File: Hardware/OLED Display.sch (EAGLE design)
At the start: 26 parts, among them J1 QWIIC_RIGHT_ANGLE, J3 QWIIC_RIGHT_ANGLE, U1 QG-2832TLBFG02

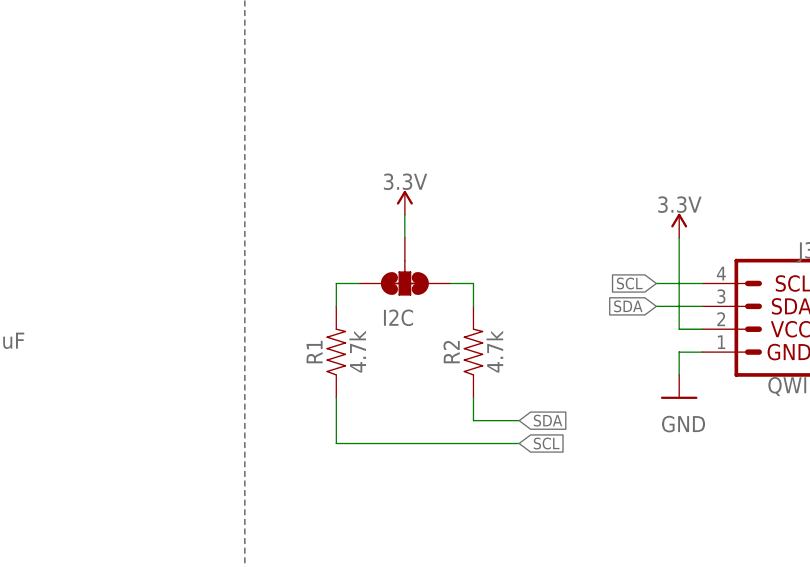
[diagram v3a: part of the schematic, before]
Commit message: Shrinks the overall size of the board
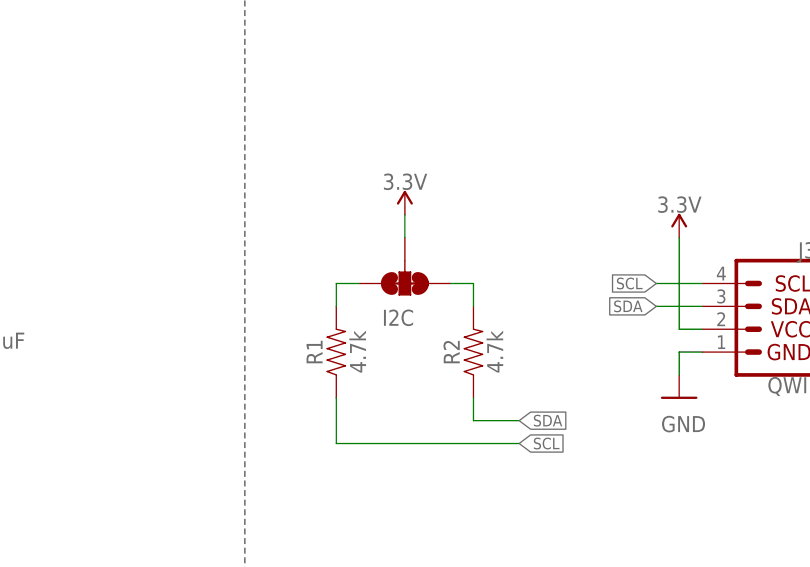
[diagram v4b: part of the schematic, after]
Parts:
- I2C: value SMT-JUMPER_3_2-NC_TRACE -> JUMPER-SMT_3_2-NC_TRACE_SILK; device NOA-Jumpers:SMT-JUMPER_3_2-NC_TRACE -> SparkFun-Jumpers:JUMPER-SMT_3_2-NC_TRACE_SILK
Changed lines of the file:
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@@
 <part name="GND8" library="SparkFun-PowerSymbols" deviceset="GND" device=""/>
 <part name="GND9" library="SparkFun-PowerSymbols" deviceset="GND" device=""/>
-<part name="I2C" library="NOA-Jumpers" deviceset="SMT-JUMPER_3_2-NC_TRACE" device=""/>
+<part name="I2C" library="SparkFun-Jumpers" deviceset="JUMPER-SMT_3_2-NC_TRACE" device="_SILK" package3d_urn="urn:adsk.eagle:package:39289/1"/>
 <part name="LOGO2" library="OSHW-LOGO-M" deviceset="OSHW-LOGO" device="MINI"/>
 <part name="FRAME2" library="SparkFun-Aesthetics" deviceset="FRAME-LETTER" device="">
@@
 will not be understood (or retained) with this version.
 </note>
+<note version="8.3" severity="warning">
+Since Version 8.3, EAGLE supports the association of 3D packages
+with devices in libraries, schematics, and board files. Those 3D
+packages will not be understood (or retained) with this version.
+</note>
 </compatibility>

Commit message: Routes the board
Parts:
- removed C3: 1.0uF, SparkFun-Capacitors:1.0UF-0603-16V-10%
- removed U1: QG-2832TLBFG02, Module:OLED-12832
- added U2: APX803S-SA, Module:APX803S-SA
- added U3: OLED_0.9"-QG-2832TLBFG02, Module:OLED_0.9"-QG-2832TLBFG02
- LOGO1: value SFE_LOGO_NAME_FLAME.2_INCH -> SFE_LOGO_NAME_FLAME.1_INCH; device SparkFun-Aesthetics:SFE_LOGO_NAME_FLAME.2_INCH -> SparkFun-Aesthetics:SFE_LOGO_NAME_FLAME.1_INCH
- R4: value 100k -> 10k; device SparkFun-Resistors:100KOHM-0603-1/10W-1% -> SparkFun-Resistors:10KOHM-0603-1/10W-1%
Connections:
- removed net N$3: C2.2, U1.C1P
- new net N$17: C2.1, U3.C2N
- net 3.3V: now also U2.VCC, U3.VBAT, U3.VDD; no longer U1.VBAT, U1.VDD
- net GND: now also U2.GND, U3.VSS; no longer C3.2, U1.VSS
- net N$1: now also C2.2, U3.C2P; no longer C1.2, U1.C2P
- net N$2: now also U3.C1N; no longer U1.C2N
- net N$4: now also C1.2, U3.C1P; no longer C2.1, U1.C1N
- net N$6: now also U3.VCOMH; no longer U1.VCOMH
- net N$7: now also U3.VCC; no longer U1.VCC
- net N$9: now also U3.IREF; no longer U1.IREF
- net RST: now also U2.!RST!, U3.RST; no longer C3.1, U1.RES#
- net SCL: now also U3.SCL; no longer U1.SCL
- net SDA: now also U3.SDA; no longer U1.SDA
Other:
- note added: "Soft Start Circuit - APX803S-SA"
- note removed: "100ms Delayed Startup"
- note removed: "Soft Start Circuit"
- moved on the sheet: C1, C2, C4, C5, C7, C8, R3, R4

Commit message: Updates the display device and footprint name, adds version in silk
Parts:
- U3: value OLED_0.9"-QG-2832TLBFG02 -> QG-2832TLBFG02; device Module:OLED_0.9"-QG-2832TLBFG02 -> Module:QG-2832TLBFG02
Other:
- moved on the sheet: C7
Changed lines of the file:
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@@
 <part name="SUPPLY6" library="SparkFun-PowerSymbols" deviceset="3.3V" device=""/>
 <part name="LOGO1" library="SparkFun-Aesthetics" deviceset="SFE_LOGO_NAME_FLAME" device=".1_INCH"/>
-<part name="U3" library="Module" deviceset="OLED_0.9&quot;-QG-2832TLBFG02" device=""/>
+<part name="U3" library="Module" deviceset="QG-2832TLBFG02" device=""/>
 <part name="GND16" library="SparkFun-PowerSymbols" deviceset="GND" device=""/>
 </parts>
@@
 <instance part="H2" gate="G$1" x="238.76" y="30.48" smashed="yes"/>
 <instance part="LOGO3" gate="G$1" x="157.48" y="40.64" smashed="yes"/>
-<instance part="C7" gate="G$1" x="27.94" y="129.54" smashed="yes" rot="MR180">
-<attribute name="NAME" x="28.321" y="133.096" size="1.778" layer="95" font="vector" rot="R270"/>
-<attribute name="VALUE" x="28.321" y="118.364" size="1.778" layer="96" font="vector" rot="MR90"/>
+<instance part="C7" gate="G$1" x="27.94" y="127" smashed="yes" rot="MR180">
+<attribute name="NAME" x="28.321" y="130.556" size="1.778" layer="95" font="vector" rot="R270"/>
+<attribute name="VALUE" x="28.321" y="115.824" size="1.778" layer="96" font="vector" rot="MR90"/>
 </instance>
 <instance part="C8" gate="G$1" x="17.78" y="144.78" smashed="yes" rot="MR180">
@@
 <attribute name="VALUE" x="22.86" y="114.046" size="1.778" layer="96" font="vector" rot="MR0" align="top-center"/>
 </instance>
-<instance part="SUPPLY1" gate="G$1" x="17.78" y="172.72" smashed="yes" rot="MR0">
-<attribute name="VALUE" x="17.78" y="175.514" size="1.778" layer="96" font="vector" rot="MR0" align="bottom-center"/>
+<instance part="SUPPLY1" gate="G$1" x="17.78" y="152.4" smashed="yes" rot="MR0">
+<attribute name="VALUE" x="17.78" y="155.194" size="1.778" layer="96" font="vector" rot="MR0" align="bottom-center"/>
 </instance>
 <instance part="SUPPLY2" gate="G$1" x="134.62" y="149.86" smashed="yes">
@@
 <attribute name="VALUE" x="35.56" y="114.046" size="1.778" layer="96" font="vector" rot="MR0" align="top-center"/>
 </instance>
-<instance part="GND6" gate="1" x="73.66" y="104.14" smashed="yes">
-<attribute name="VALUE" x="73.66" y="103.886" size="1.778" layer="96" font="vector" align="top-center"/>
+<instance part="GND6" gate="1" x="73.66" y="114.3" smashed="yes">
+<attribute name="VALUE" x="73.66" y="114.046" size="1.778" layer="96" font="vector" align="top-center"/>
 </instance>
 <instance part="GND7" gate="1" x="17.78" y="114.3" smashed="yes" rot="MR0">
@@
 <segment>
 <pinref part="C7" gate="G$1" pin="1"/>
-<wire x1="27.94" y1="124.46" x2="27.94" y2="116.84" width="0.1524" layer="91"/>
+<wire x1="27.94" y1="121.92" x2="27.94" y2="116.84" width="0.1524" layer="91"/>
 <pinref part="GND4" gate="1" pin="GND"/>
 </segment>
@@
 <pinref part="GND6" gate="1" pin="GND"/>
 <pinref part="R3" gate="G$1" pin="1"/>
-<wire x1="73.66" y1="119.38" x2="73.66" y2="106.68" width="0.1524" layer="91"/>
+<wire x1="73.66" y1="119.38" x2="73.66" y2="116.84" width="0.1524" layer="91"/>
 </segment>
 <segment>
@@
 <net name="N$7" class="0">
 <segment>
-<wire x1="27.94" y1="134.62" x2="27.94" y2="132.08" width="0.1524" layer="91"/>
+<wire x1="27.94" y1="134.62" x2="27.94" y2="129.54" width="0.1524" layer="91"/>
 <pinref part="C7" gate="G$1" pin="2"/>
 <pinref part="U3" gate="G$1" pin="VCC"/>
@@
 <wire x1="17.78" y1="147.32" x2="17.78" y2="149.86" width="0.1524" layer="91" style="longdash"/>
 <junction x="17.78" y="149.86"/>
-<wire x1="17.78" y1="172.72" x2="17.78" y2="149.86" width="0.1524" layer="91"/>
+<wire x1="17.78" y1="152.4" x2="17.78" y2="149.86" width="0.1524" layer="91"/>
 <pinref part="SUPPLY1" gate="G$1" pin="3.3V"/>
 <pinref part="U3" gate="G$1" pin="VDD"/>

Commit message: Adds testpoints
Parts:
- added TP1, TP2, TP3, TP4: TEST-POINT3X4, SparkFun-Connectors:TEST-POINT3X4
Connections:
- net 3.3V: now also TP3.1
- net GND: now also TP4.1
- net SCL: now also TP1.1
- net SDA: now also TP2.1
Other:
- note added: "Testpoints"
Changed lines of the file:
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@@
 <part name="U3" library="Module" deviceset="QG-2832TLBFG02" device=""/>
 <part name="GND16" library="SparkFun-PowerSymbols" deviceset="GND" device=""/>
+<part name="TP1" library="SparkFun-Connectors" deviceset="TEST-POINT" device="3X4"/>
+<part name="TP2" library="SparkFun-Connectors" deviceset="TEST-POINT" device="3X4"/>
+<part name="TP3" library="SparkFun-Connectors" deviceset="TEST-POINT" device="3X4"/>
+<part name="TP4" library="SparkFun-Connectors" deviceset="TEST-POINT" device="3X4"/>
+<part name="SUPPLY7" library="SparkFun-PowerSymbols" deviceset="3.3V" device=""/>
+<part name="GND2" library="SparkFun-PowerSymbols" deviceset="GND" device=""/>
 </parts>
 <sheets>
@@
 <text x="149.86" y="7.62" size="2.54" layer="94" font="vector">Revised By: Elias Santistevan</text>
 <wire x1="116.84" y1="185.42" x2="116.84" y2="99.06" width="0.1524" layer="97" style="longdash"/>
-<wire x1="116.84" y1="99.06" x2="116.84" y2="0" width="0.1524" layer="97" style="longdash"/>
+<wire x1="116.84" y1="99.06" x2="116.84" y2="58.42" width="0.1524" layer="97" style="longdash"/>
+<wire x1="116.84" y1="58.42" x2="116.84" y2="0" width="0.1524" layer="97" style="longdash"/>
 <wire x1="0" y1="99.06" x2="116.84" y2="99.06" width="0.1524" layer="97" style="longdash"/>
-<wire x1="116.84" y1="99.06" x2="248.92" y2="99.06" width="0.1524" layer="97" style="longdash"/>
+<wire x1="116.84" y1="99.06" x2="160.02" y2="99.06" width="0.1524" layer="97" style="longdash"/>
 <text x="182.88" y="177.8" size="2.54" layer="94" font="vector" align="center">Qwiic Connectors</text>
 <text x="60.96" y="180.34" size="2.54" layer="94" font="vector" align="center">OLED Display - QG-2832TLBFG02</text>
 <text x="60.96" y="91.44" size="2.54" layer="94" font="vector" align="center">Soft Start Circuit - APX803S-SA</text>
+<text x="129.54" y="91.44" size="2.54" layer="94" font="vector">Testpoints</text>
+<wire x1="160.02" y1="99.06" x2="248.92" y2="99.06" width="0.1524" layer="97" style="longdash"/>
+<wire x1="116.84" y1="58.42" x2="160.02" y2="58.42" width="0.2032" layer="97" style="longdash"/>
+<wire x1="160.02" y1="58.42" x2="160.02" y2="99.06" width="0.2032" layer="97" style="longdash"/>
 </plain>
 <instances>
@@
 <attribute name="VALUE" x="43.18" y="114.046" size="1.778" layer="96" font="vector" rot="MR0" align="top-center"/>
 </instance>
+<instance part="TP1" gate="G$1" x="139.7" y="78.74" smashed="yes">
+<attribute name="NAME" x="144.78" y="78.74" size="1.778" layer="95" font="vector"/>
+</instance>
+<instance part="TP2" gate="G$1" x="139.7" y="76.2" smashed="yes">
+<attribute name="NAME" x="144.78" y="76.2" size="1.778" layer="95" font="vector"/>
+</instance>
+<instance part="TP3" gate="G$1" x="139.7" y="73.66" smashed="yes">
+<attribute name="NAME" x="144.78" y="73.66" size="1.778" layer="95" font="vector"/>
+</instance>
+<instance part="TP4" gate="G$1" x="139.7" y="71.12" smashed="yes">
+<attribute name="NAME" x="144.78" y="71.12" size="1.778" layer="95" font="vector"/>
+</instance>
+<instance part="SUPPLY7" gate="G$1" x="137.16" y="81.28" smashed="yes">
+<attribute name="VALUE" x="137.16" y="84.074" size="1.778" layer="96" font="vector" align="bottom-center"/>
+</instance>
+<instance part="GND2" gate="1" x="137.16" y="66.04" smashed="yes">
+<attribute name="VALUE" x="137.16" y="65.786" size="1.778" layer="96" font="vector" align="top-center"/>
+</instance>
 </instances>
 <busses>
@@
 <pinref part="GND16" gate="1" pin="GND"/>
 </segment>
+<segment>
+<pinref part="TP4" gate="G$1" pin="1"/>
+<wire x1="139.7" y1="71.12" x2="137.16" y2="71.12" width="0.1524" layer="91"/>
+<pinref part="GND2" gate="1" pin="GND"/>
+<wire x1="137.16" y1="71.12" x2="137.16" y2="68.58" width="0.1524" layer="91"/>
+</segment>
 </net>
 <net name="SCL" class="0">
@@
 <label x="162.56" y="142.24" size="1.27" layer="95" font="vector" rot="R180" xref="yes"/>
 </segment>
+<segment>
+<pinref part="TP1" gate="G$1" pin="1"/>
+<wire x1="139.7" y1="78.74" x2="134.62" y2="78.74" width="0.1524" layer="91"/>
+<label x="134.62" y="78.74" size="1.27" layer="95" rot="R180" xref="yes"/>
+</segment>
 </net>
 <net name="SDA" class="0">
@@
 <wire x1="167.64" y1="139.7" x2="162.56" y2="139.7" width="0.1524" layer="91"/>
 <label x="162.56" y="139.7" size="1.27" layer="95" font="vector" rot="R180" xref="yes"/>
+</segment>
+<segment>
+<pinref part="TP2" gate="G$1" pin="1"/>
+<wire x1="139.7" y1="76.2" x2="134.62" y2="76.2" width="0.1524" layer="91"/>
+<label x="134.62" y="76.2" size="1.27" layer="95" rot="R180" xref="yes"/>
 </segment>
 </net>
@@
 <pinref part="SUPPLY6" gate="G$1" pin="3.3V"/>
 </segment>
-</net>
+<segment>
+<pinref part="SUPPLY7" gate="G$1" pin="3.3V"/>
+<pinref part="TP3" gate="G$1" pin="1"/>
+<wire x1="139.7" y1="73.66" x2="137.16" y2="73.66" width="0.1524" layer="91"/>
+<wire x1="137.16" y1="73.66" x2="137.16" y2="81.28" width="0.1524" layer="91"/>
+</segment>
+</net>

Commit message: Adds more datasheets, updates part number for OLED display
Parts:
- U3: value QG-2832TLBFG02 -> AMO091-12832BFG02-H14; device Module:QG-2832TLBFG02 -> Module:AMO091-12832BFG02-H14
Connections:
- removed net RST: R4.1, U2.!RST!, U3.RST
- new net !RST!: R4.1, U2.!RST!, U3.!RST!
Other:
- note added: "OLED Display AMO091-12832BFG02-H14"
- note removed: "OLED Display - QG-2832TLBFG02"
- moved on the sheet: R3
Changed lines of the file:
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@@
 <part name="SUPPLY6" library="SparkFun-PowerSymbols" deviceset="3.3V" device=""/>
 <part name="LOGO1" library="SparkFun-Aesthetics" deviceset="SFE_LOGO_NAME_FLAME" device=".1_INCH"/>
-<part name="U3" library="Module" deviceset="QG-2832TLBFG02" device=""/>
+<part name="U3" library="Module" deviceset="AMO091-12832BFG02-H14" device=""/>
 <part name="GND16" library="SparkFun-PowerSymbols" deviceset="GND" device=""/>
 <part name="TP1" library="SparkFun-Connectors" deviceset="TEST-POINT" device="3X4"/>
@@
 <wire x1="116.84" y1="99.06" x2="160.02" y2="99.06" width="0.1524" layer="97" style="longdash"/>
 <text x="182.88" y="177.8" size="2.54" layer="94" font="vector" align="center">Qwiic Connectors</text>
-<text x="60.96" y="180.34" size="2.54" layer="94" font="vector" align="center">OLED Display - QG-2832TLBFG02</text>
+<text x="60.96" y="177.8" size="2.54" layer="94" font="vector" align="center">OLED Display
+AMO091-12832BFG02-H14
+</text>
 <text x="60.96" y="91.44" size="2.54" layer="94" font="vector" align="center">Soft Start Circuit - APX803S-SA</text>
 <text x="129.54" y="91.44" size="2.54" layer="94" font="vector">Testpoints</text>
@@
 <attribute name="VALUE" x="143.764" y="134.62" size="1.778" layer="96" font="vector" rot="R90" align="top-center"/>
 </instance>
-<instance part="R3" gate="G$1" x="73.66" y="124.46" smashed="yes" rot="R90">
-<attribute name="NAME" x="74.422" y="129.54" size="1.778" layer="95" font="vector" rot="R270" align="bottom-center"/>
-<attribute name="VALUE" x="76.2" y="118.364" size="1.778" layer="96" font="vector" rot="R270" align="top-center"/>
+<instance part="R3" gate="G$1" x="81.28" y="124.46" smashed="yes" rot="R90">
+<attribute name="NAME" x="82.042" y="129.54" size="1.778" layer="95" font="vector" rot="R270" align="bottom-center"/>
+<attribute name="VALUE" x="83.82" y="118.364" size="1.778" layer="96" font="vector" rot="R270" align="top-center"/>
 </instance>
 <instance part="C5" gate="G$1" x="35.56" y="124.46" smashed="yes" rot="MR0">
@@
 <attribute name="VALUE" x="35.56" y="114.046" size="1.778" layer="96" font="vector" rot="MR0" align="top-center"/>
 </instance>
-<instance part="GND6" gate="1" x="73.66" y="114.3" smashed="yes">
-<attribute name="VALUE" x="73.66" y="114.046" size="1.778" layer="96" font="vector" align="top-center"/>
+<instance part="GND6" gate="1" x="81.28" y="114.3" smashed="yes">
+<attribute name="VALUE" x="81.28" y="114.046" size="1.778" layer="96" font="vector" align="top-center"/>
 </instance>
 <instance part="GND7" gate="1" x="17.78" y="114.3" smashed="yes" rot="MR0">
@@
 <instance part="U3" gate="G$1" x="58.42" y="139.7" smashed="yes">
 <attribute name="NAME" x="48.26" y="152.4" size="1.778" layer="95" font="vector"/>
-<attribute name="VALUE" x="48.26" y="124.46" size="1.778" layer="96" font="vector"/>
+<attribute name="VALUE" x="45.72" y="124.46" size="1.778" layer="96" font="vector"/>
 </instance>
 <instance part="GND16" gate="1" x="43.18" y="114.3" smashed="yes" rot="MR0">
@@
 <segment>
 <pinref part="R3" gate="G$1" pin="2"/>
-<wire x1="71.12" y1="132.08" x2="73.66" y2="132.08" width="0.1524" layer="91"/>
-<wire x1="73.66" y1="132.08" x2="73.66" y2="129.54" width="0.1524" layer="91"/>
+<wire x1="71.12" y1="132.08" x2="81.28" y2="132.08" width="0.1524" layer="91"/>
+<wire x1="81.28" y1="132.08" x2="81.28" y2="129.54" width="0.1524" layer="91"/>
 <pinref part="U3" gate="G$1" pin="IREF"/>
 </segment>
@@
 <pinref part="GND6" gate="1" pin="GND"/>
 <pinref part="R3" gate="G$1" pin="1"/>
-<wire x1="73.66" y1="119.38" x2="73.66" y2="116.84" width="0.1524" layer="91"/>
+<wire x1="81.28" y1="119.38" x2="81.28" y2="116.84" width="0.1524" layer="91"/>
 </segment>
 <segment>
@@
 </segment>
 </net>
-<net name="RST" class="0">
+<net name="!RST!" class="0">
 <segment>
 <wire x1="73.66" y1="149.86" x2="71.12" y2="149.86" width="0.1524" layer="91"/>
 <label x="73.66" y="149.86" size="1.27" layer="95" font="vector" xref="yes"/>
-<pinref part="U3" gate="G$1" pin="RST"/>
+<pinref part="U3" gate="G$1" pin="!RST!"/>
 </segment>
 <segment>
@@
 </drawing>
 <compatibility>
+<note version="6.3" minversion="6.2.2" severity="warning">
+Since Version 6.2.2 text objects can contain more than one line,
+which will not be processed correctly with this version.
+</note>
 <note version="8.3" severity="warning">
 Since Version 8.3, EAGLE supports URNs for individual library
